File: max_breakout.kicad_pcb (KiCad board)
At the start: 4 copper layers, 51.8 x 25.9 mm, 45 parts, among them J1 Left, J2 Right, J3 AVR-JTAG-10, J4 USB_B_Micro, Q1 IRLML6402, SW1 Reset, SW2 User, SW3 User DIP Switch, SW4 ENA Switch, U1 AP7381-33SA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

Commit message: more routing
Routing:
- net /~RST: track 10.1 -> 39.8 mm, vias 2 -> 3
- net /TDI: track 15.8 -> 41.3 mm, vias 1 -> 3
- net /R3: track 2.69 -> 18.4 mm, vias 0 -> 3
- net /R7: track 2.94 -> 18.2 mm, vias 0 -> 3
- net /CLK2: track 0.00 -> 15.0 mm, vias 0 -> 1
- net /R5: track 2.81 -> 17.2 mm, vias 0 -> 3
- net /A7: track 16.1 -> 30.4 mm, vias 2 -> 6
- net /A1: track 23.9 -> 37.9 mm, vias 1 -> 2
- net /A8: track 14.8 -> 28.6 mm, vias 2 -> 4
- net /OE1: track 23.9 -> 36.0 mm
- net /A6: track 16.3 -> 28.1 mm, vias 1 -> 3
- net Net-(C12-Pad1): track 0.00 -> 10.7 mm, vias 0 -> 1
- net /A2: track 20.6 -> 30.5 mm, vias 1 -> 2
- net Net-(D3-Pad3): track 0.00 -> 9.13 mm, vias 0 -> 1
- net /A3: track 17.6 -> 26.7 mm, vias 1 -> 2
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
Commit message: updated routing and gerbers
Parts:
- moved U7 4.32 mm to (129.8, 105.2)
- moved R6 0.96 mm to (160.7, 117.3)
- moved D1 0.92 mm to (160.6, 117.2)
- moved D2 0.51 mm to (146.8, 117.2)
- moved R8 0.51 mm to (146.8, 117.2)
- moved C1 0.51 mm to (125.0, 108.8), turned to 180 degrees
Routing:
- net +3V3: track 11.8 -> 20.1 mm
- net /3V3_out: track 22.9 -> 15.3 mm, vias 3 -> 1
- net GND: track 61.8 -> 66.3 mm, vias 25 -> 27
- net Net-(Q1-Pad1): track 0.00 -> 4.07 mm
- net Net-(D2-Pad1): track 0.00 -> 1.87 mm, vias 0 -> 1
- net /CLK: track 2.83 -> 3.58 mm
- net /~RST: track 39.8 -> 39.1 mm
- net VCC: track 54.7 -> 54.0 mm
- net /A1: track 37.9 -> 37.3 mm
- net Net-(C13-Pad1): track 18.4 -> 18.9 mm
- net /OE1: track 36.0 -> 35.5 mm
- net Net-(D2-Pad2): track 5.89 -> 6.40 mm

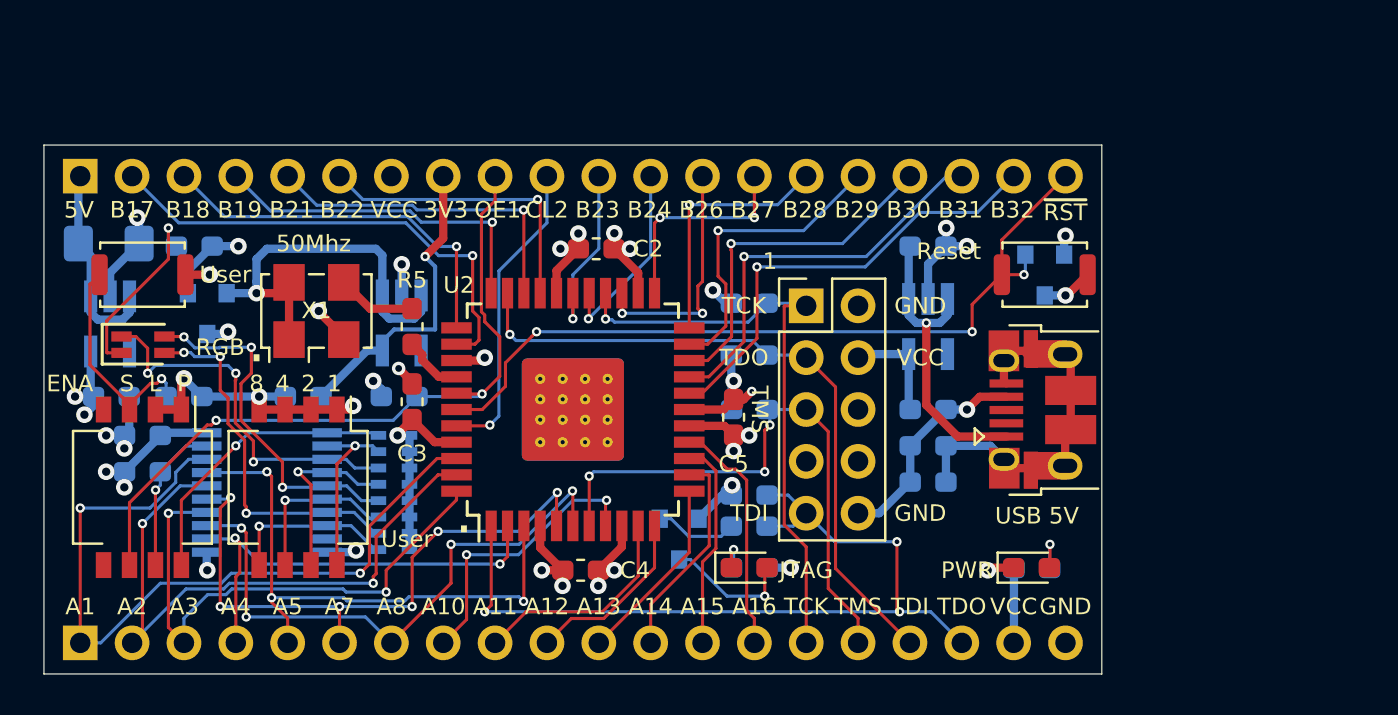
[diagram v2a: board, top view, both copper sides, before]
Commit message: fixed dip switch footprints, separated component vcc's
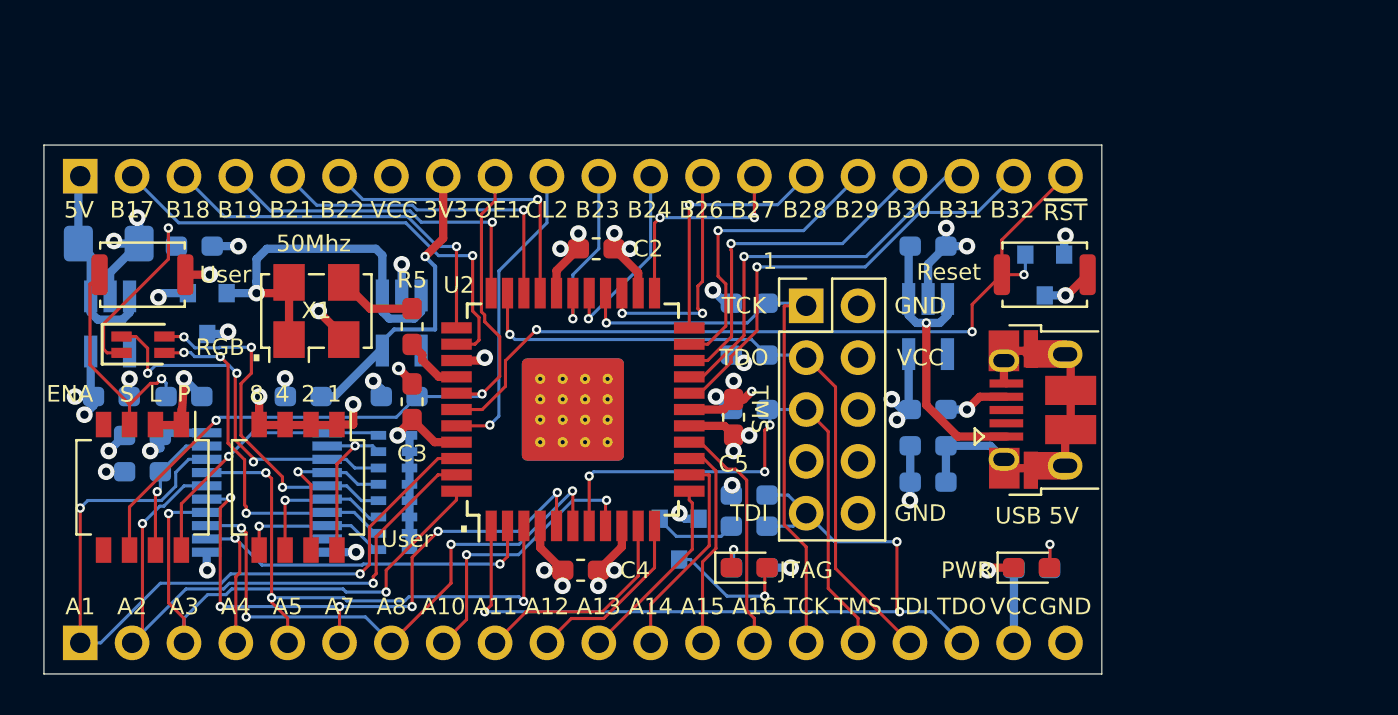
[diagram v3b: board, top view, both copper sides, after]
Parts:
- C10: value .33uF -> 2.2uF
- SW3, SW4: footprint Button_Switch_SMD:SW_DIP_SPSTx04_Slide_KingTek_DSHP04TS_W7.62mm_P1.27mm -> Button_Switch_SMD:SW_DIP_SPSTx04_Slide_Omron_A6H-4101_W6.15mm_P1.27mm
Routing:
- net VCC: track 54.0 -> 47.9 mm, vias 15 -> 21
- net GND: track 66.3 -> 61.9 mm, vias 27 -> 30
- net /OE1: track 35.5 -> 34.6 mm
- net /R1: track 14.3 -> 13.4 mm
- net Net-(C12-Pad1): track 10.7 -> 11.4 mm
- net /R6: track 8.33 -> 7.60 mm
- net /R4: track 9.03 -> 8.29 mm
- net /R2: track 8.85 -> 8.11 mm
- net /R8: track 8.25 -> 7.51 mm
- net Net-(R15-Pad2): track 7.46 -> 6.85 mm

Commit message: better part alignment
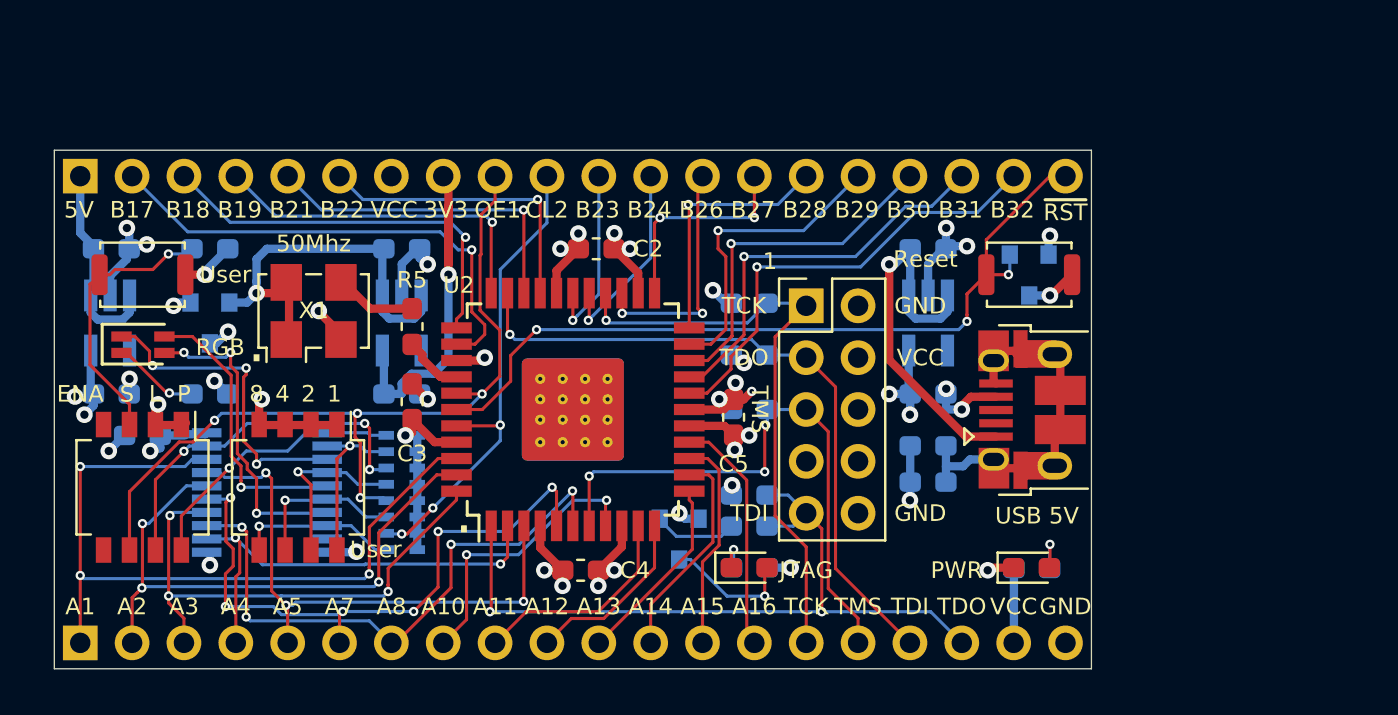
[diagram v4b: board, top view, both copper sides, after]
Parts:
- removed C6: 100uF, Capacitor_SMD:C_1206_3216Metric_Pad1.42x1.75mm_HandSolder
- removed R15, R9: 10K, Resistor_SMD:R_0603_1608Metric_Pad1.05x0.95mm_HandSolder
- added C11: .33uF, Capacitor_SMD:C_0603_1608Metric_Pad1.05x0.95mm_HandSolder, B.Cu at (115.6, 101.6)
- added C14: .33uF, Capacitor_SMD:C_0603_1608Metric_Pad1.05x0.95mm_HandSolder, B.Cu at (129.8, 101.6)
- RN1: value R_Network08 -> 10K
- U4, U5, U7: value MAX40200AUK -> MAX40203AUK+T
- moved C12 7.35 mm to (120.4, 101.6)
- moved R18 7.28 mm to (120.4, 108.7)
- moved C1 4.83 mm to (129.8, 108.7), turned to 0 degrees
- moved C10 0.76 mm to (155.6, 108.7)
- moved SW1 0.76 mm to (160.5, 102.9)
- moved U3 0.76 mm to (160.5, 102.9)
- moved J4 0.51 mm to (160.7, 109.5)
- moved U1 0.48 mm to (120.4, 105.2)
- moved RN1 0.38 mm to (129.8, 113.5)
- moved U4 0.17 mm to (155.6, 105.2)
- moved X1 0.14 mm to (125.5, 104.6)
- moved C8 0.13 mm to (155.6, 101.6)
- moved C9 0.13 mm to (115.6, 108.7)
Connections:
- D3 pad 1: /R3 -> Net-(D3-Pad1)
- D3 pad 2: /R5 -> Net-(D3-Pad2)
- D3 pad 4: /R7 -> Net-(D3-Pad4)
- RN1 pad 10: /R7 -> /CLK2
- RN1 pad 12: /R5 -> /OE1
- SW4 pad 7: Net-(R15-Pad2) -> /R3
- U6 pad 19: Net-(R15-Pad2) -> /R3
- U6 pad 3: /R3 -> Net-(D3-Pad1)
- U6 pad 5: /R5 -> Net-(D3-Pad2)
- U6 pad 7: /R7 -> Net-(D3-Pad4)
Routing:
- net /R7: track 17.9 -> 0.00 mm, vias 3 -> 0
- net /R5: track 17.4 -> 0.00 mm, vias 3 -> 0
- net Net-(D3-Pad1): track 0.00 -> 15.7 mm, vias 0 -> 3
- net Net-(D3-Pad4): track 0.00 -> 15.3 mm, vias 0 -> 3
- net Net-(D3-Pad2): track 0.00 -> 14.0 mm, vias 0 -> 1
- net /CLK2: track 15.0 -> 23.6 mm, vias 1 -> 3
- net Net-(R15-Pad2): track 6.85 -> 0.00 mm, vias 1 -> 0
- net /OE1: track 34.6 -> 40.6 mm, vias 2 -> 4
- net Net-(D3-Pad3): track 9.26 -> 4.29 mm
- net Net-(C8-Pad1): track 15.0 -> 18.9 mm
- net /TDI: track 41.3 -> 37.6 mm, vias 3 -> 2
- net /3V3_out: track 15.3 -> 18.7 mm
- net VCC: track 47.9 -> 44.6 mm, vias 21 -> 19
- net GND: track 61.9 -> 59.7 mm, vias 30 -> 29
- net Net-(C12-Pad1): track 11.4 -> 13.4 mm
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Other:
- board size 51.8 x 25.9 mm -> 50.8 x 25.4 mm
- net class Default: clearance 0.127 -> 0.1524; trace_width 0.127 -> 0.1524
- net class Power: via_dia 0.4572 -> 0.8128; via_drill 0.2286 -> 0.4064
- rule trace_clearance: 0.127 -> 0.1524
- rule trace_min: 0.127 -> 0.1524
- board text added: "EPM7032STC44"

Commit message: aligned traces
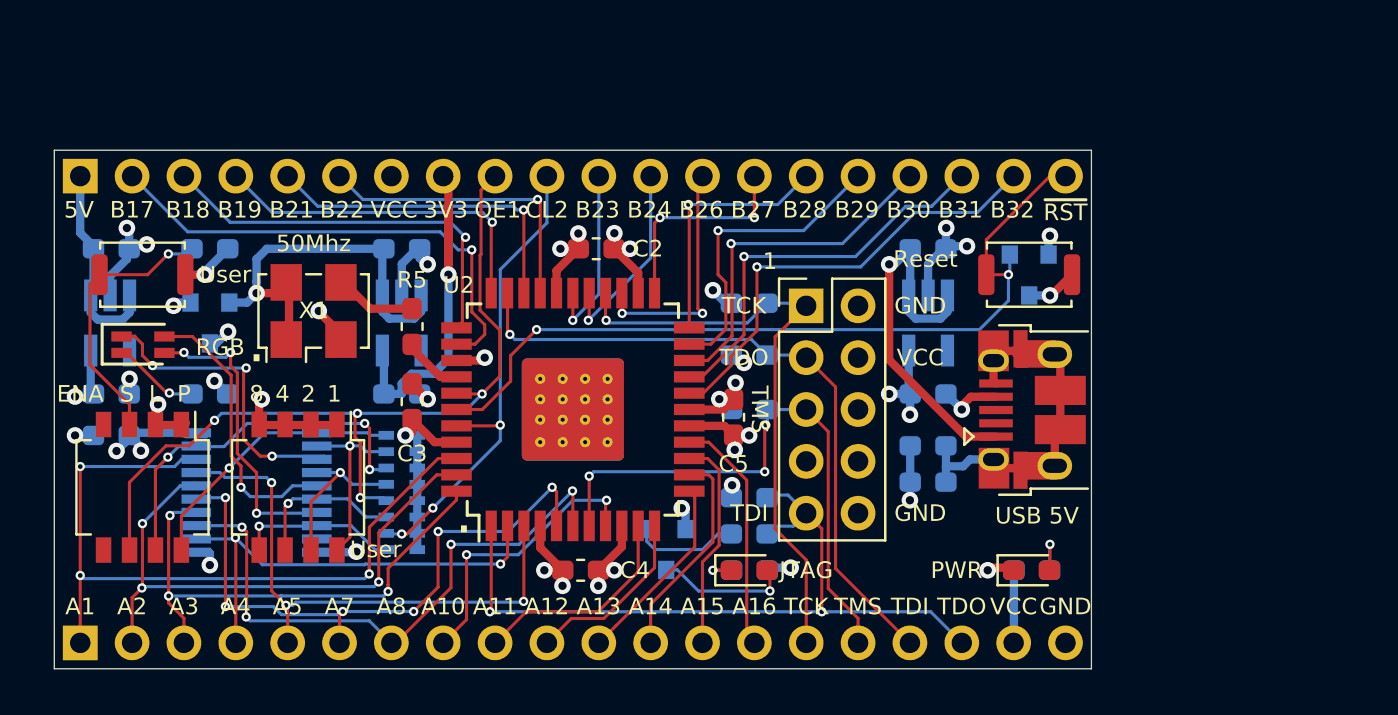
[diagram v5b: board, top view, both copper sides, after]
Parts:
- moved C7 1.52 mm to (115.6, 110.7)
- moved Q1 0.81 mm to (142.7, 116.3)
- moved U6 0.51 mm to (122.7, 113.5)
- moved R7 0.38 mm to (146.8, 115.6)
- moved D1 0.13 mm to (160.6, 117.3)
- moved D2 0.13 mm to (146.8, 117.3)
- moved R4 0.13 mm to (146.8, 113.8)
- moved R8 0.13 mm to (146.8, 117.3)
- moved R6 0.09 mm to (160.7, 117.3)
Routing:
- net VCC: track 44.6 -> 46.5 mm, vias 19 -> 18
- net Net-(Q1-Pad1): track 4.10 -> 5.93 mm
- net /~RST: track 38.4 -> 39.5 mm, vias 3 -> 2
- net GND: track 59.7 -> 58.7 mm, vias 29 -> 28
- net /A7: track 30.9 -> 30.2 mm
- net /R4: track 8.68 -> 8.03 mm
- net Net-(D3-Pad1): track 15.7 -> 15.1 mm

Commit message: version 2.0
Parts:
- R18: moved to F.Cu
- moved C7 18.1 mm to (132.1, 103.4), turned to 0 degrees
- moved R18 13.9 mm to (132.1, 101.1)
- moved C4 12.8 mm to (150.2, 112.0)
- moved U2 12.8 mm to (149.9, 104.1)
- moved C9 12.8 mm to (127.3, 103.4)
- moved U1 12.8 mm to (132.1, 99.9)
- moved U6 12.8 mm to (134.4, 108.2)
- moved C11 12.8 mm to (127.3, 96.3)
- moved C12 12.8 mm to (132.1, 96.3)
- moved C1 12.8 mm to (141.5, 103.4)
- moved C10 12.8 mm to (167.3, 103.4)
- moved C3 12.8 mm to (142.0, 103.8)
- moved C5 12.8 mm to (157.7, 104.5)
- moved D1 12.8 mm to (172.3, 112.0)
- moved D2 12.8 mm to (158.5, 112.0)
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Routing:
- net Net-(D3-Pad3): track 4.29 -> 7.58 mm, vias 1 -> 2
- net Net-(D3-Pad4): track 15.3 -> 13.0 mm, vias 3 -> 1
- net Net-(D3-Pad2): track 14.4 -> 12.3 mm
- net VCC: track 46.5 -> 44.8 mm
- net /~RST: track 39.5 -> 38.3 mm
- net GND: track 58.7 -> 59.8 mm, vias 28 -> 30
- net /A8: track 28.8 -> 29.8 mm
- net /A3: track 25.6 -> 26.3 mm
- net /TMS: track 28.7 -> 28.1 mm
- net Net-(D3-Pad1): track 15.1 -> 15.6 mm

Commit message: straighten traces
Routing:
- net GND: track 59.8 -> 60.4 mm, vias 30 -> 31
- added copper zone on B.Cu, net GND
- added copper zone on F.Cu, net GND

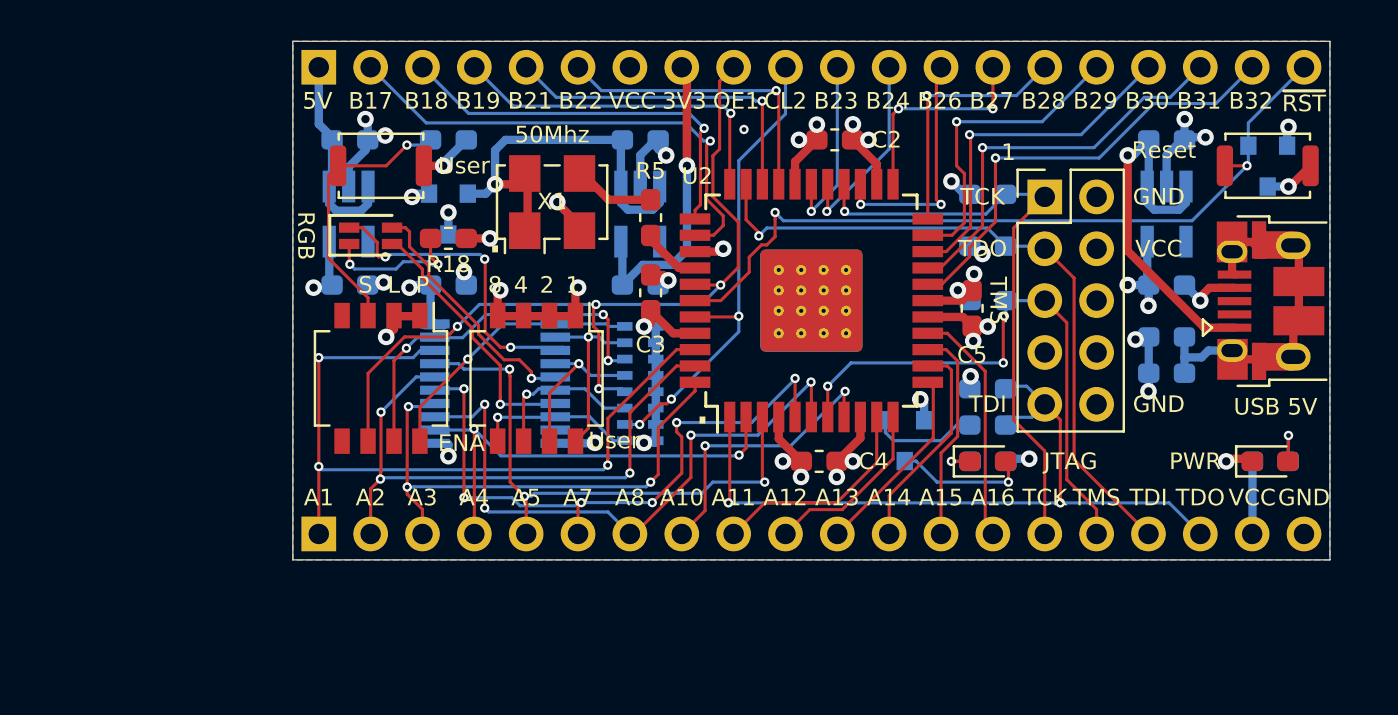
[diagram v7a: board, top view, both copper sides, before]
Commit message: fixed up gnd planes
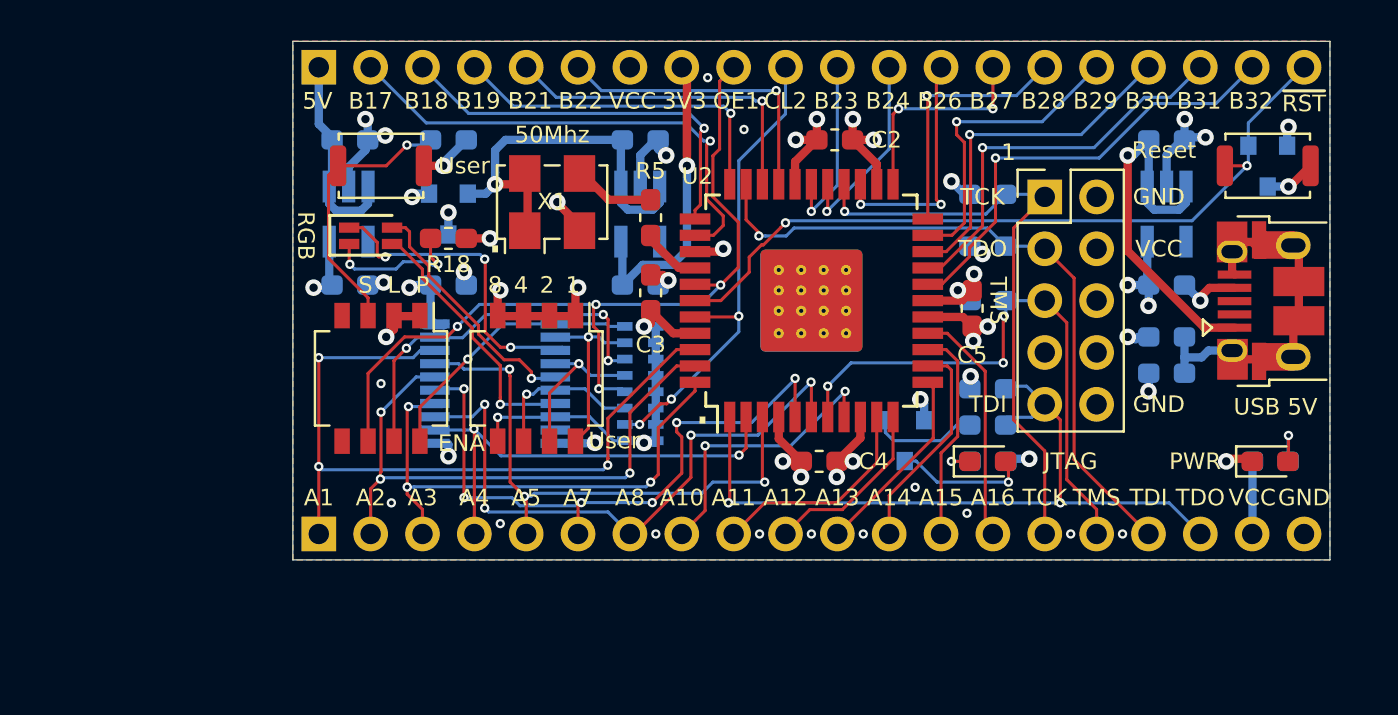
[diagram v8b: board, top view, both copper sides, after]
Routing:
- net GND: track 60.4 -> 58.6 mm, vias 31 -> 43
- net /~RST: track 38.3 -> 37.3 mm
